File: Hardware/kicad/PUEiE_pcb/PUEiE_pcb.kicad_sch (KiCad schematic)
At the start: 11 parts, among them J1 Screw_Terminal_01x02, SW1 SW_DPDT_x2, U1 LM2675M-3.3, U2 MAX-M10S

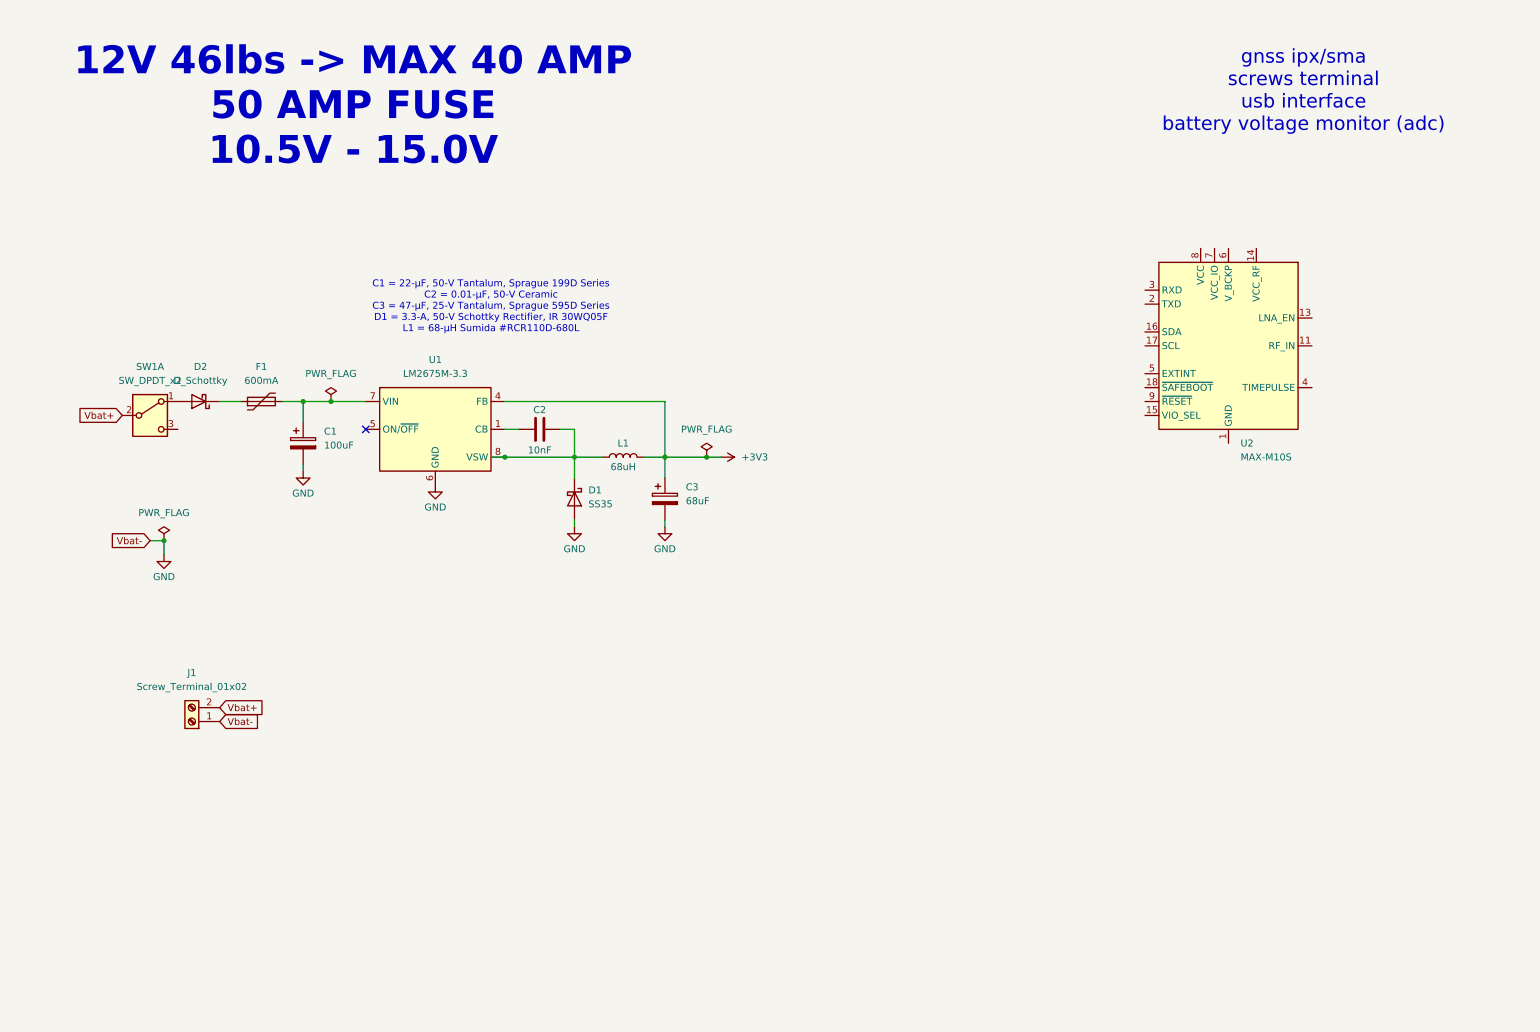
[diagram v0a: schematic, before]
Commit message: tps563240, GNSS
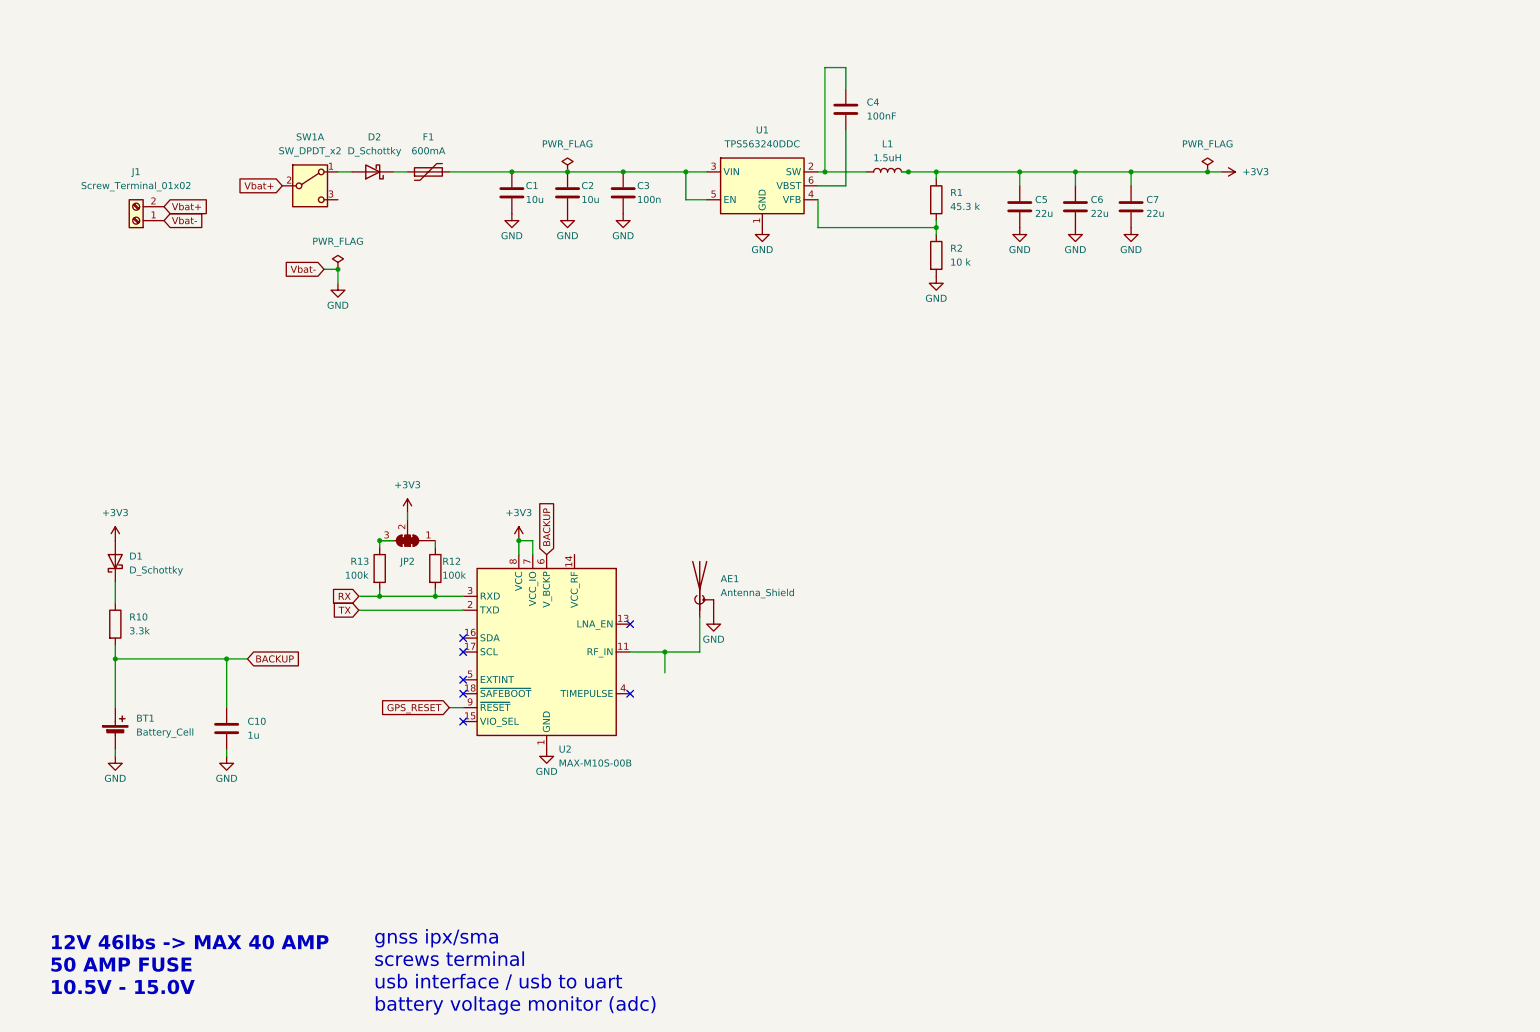
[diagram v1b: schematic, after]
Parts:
- removed C1: 100uF, symbol Device:C_Polarized
- removed C3: 68uF, symbol Device:C_Polarized
- removed D1: SS35, Diode_SMD:D_SMA, symbol Diode:SS35
- removed U1: LM2675M-3.3, Package_SO:SOIC-8_3.9x4.9mm_P1.27mm, symbol Regulator_Switching:LM2675M-3.3
- added AE1: Antenna_Shield, symbol Device:Antenna_Shield
- added BT1: Battery_Cell, symbol Device:Battery_Cell
- added C1: 10u, Capacitor_SMD:C_0805_2012Metric, symbol Device:C
- added C10: 1u, Capacitor_SMD:C_0805_2012Metric, symbol Device:C
- added C3: 100n, Capacitor_SMD:C_0805_2012Metric, symbol Device:C
- added C4: 100nF, Capacitor_SMD:C_0603_1608Metric, symbol Device:C
- added C5, C6, C7: 22u, Capacitor_SMD:C_0603_1608Metric, symbol Device:C
- added D1: D_Schottky, Diode_SMD:D_SOD-882, symbol Device:D_Schottky
- added JP2: SolderJumper_3_Bridged123, symbol Jumper:SolderJumper_3_Bridged123
- added R1: 45.3 k, Resistor_SMD:R_0402_1005Metric, symbol Device:R
- added R10: 3.3k, Resistor_SMD:R_0805_2012Metric, symbol Device:R
- added R12, R13: 100k, Resistor_SMD:R_0805_2012Metric, symbol Device:R
- added R2: 10 k, Resistor_SMD:R_0201_0603Metric, symbol Device:R
- added U1: TPS563240DDC, Package_TO_SOT_SMD:SOT-23-6, symbol Regulator_Switching:TPS563240DDC
- C2: value 10nF -> 10u; footprint (none) -> Capacitor_SMD:C_0805_2012Metric
- L1: value 68uH -> 1.5uH; Link 1 (none) -> https://jlcpcb.com/partdetail/Sumida-104CDMCCDS1R5MC/C516064
- U2: value MAX-M10S -> MAX-M10S-00B; Link 1 (none) -> https://jlcpcb.com/partdetail/UBLOX-MAX_M10S00B/C4153167
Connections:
- net +3V3: now also U2.7 (VCC_IO), U2.8 (VCC), C5.1, C6.1, C7.1, D1.2 (A), JP2.2 (C), R1.1
- net GND: now also C2.2, U2.1 (GND), U2.10 (GND), U2.12 (GND), AE1.2 (Shield), BT1.2 (-), C1.2, C10.2, C3.2, C5.2, C6.2, C7.2, R2.2, U1.1 (GND)
- net at L1.1: now also C4.1, U1.2 (SW); no longer C2.2
- net at U2.11 (RF_IN): now also AE1.1 (A)
- net TX: now reaches U2.2 (TXD)
- net RX: now reaches U2.3 (RXD)
- net RX: now also R12.2, R13.2
- net BACKUP: now reaches U2.6 (V_BCKP)
- net BACKUP: now also BT1.1 (+), C10.1, R10.2
- net GPS_RESET: now reaches U2.9 (~{RESET})
- net at C2.1: now also F1.2, C1.1, C3.1, U1.3 (VIN), U1.5 (EN)
- new net: R1.2, R2.1, U1.4 (VFB)
- new net: C4.2, U1.6 (VBST)
- new net: D1.1 (K), R10.1
- new net: JP2.1 (A), R12.1
- new net: JP2.3 (B), R13.1
- no-connect marks 1 -> 7
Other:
- note added: "gnss ipx/sma screws terminal usb interface / usb to uart battery voltage monitor (adc)"
- note removed: "C1 = 22-μF, 50-V Tantalum, Sprague 199D Series C2 = 0.01-μF, 50-V Ceramic C3 = 47-μF, 25-V Tantalum, Sprague 595D Series D1 = 3.3-A, 50-V Schottky Rectifier, IR 30WQ05F L1 = 68-μH Sumida #RCR110D-680L"
- note removed: "gnss ipx/sma screws terminal usb interface battery voltage monitor (adc)"
- moved on the sheet: D2, F1, J1, SW1A, U2

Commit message: usbc
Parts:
- removed JP2: SolderJumper_3_Bridged123, symbol Jumper:SolderJumper_3_Bridged123
- added C8: 22uF, symbol Device:C
- added J2: USB_C_Receptacle_USB2.0_14P, symbol Connector:USB_C_Receptacle_USB2.0_14P
- added JP1: SolderJumper_3_Bridged123, symbol Jumper:SolderJumper_3_Bridged123
- added R3, R4: 5.1k, symbol Device:R
- added U3: USBLC6-2P6, Package_TO_SOT_SMD:SOT-666, symbol Power_Protection:USBLC6-2P6
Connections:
- net +3V3: now also JP1.2 (C)
- net GND: now also C8.1, J2.A1 (GND), J2.A12 (GND), J2.B1 (GND), J2.B12 (GND), J2.S1 (SHIELD), R3.2, R4.2, U3.2 (GND)
- net RX: no longer R12.2
- net TX: now also R12.2
- net at R12.1: now also JP1.1 (A)
- net at R13.1: now also JP1.3 (B)
- new net: C8.2, J2.A4 (VBUS), J2.A9 (VBUS), J2.B4 (VBUS), J2.B9 (VBUS)
- new net: J2.A5 (CC1), R4.1
- new net: J2.B5 (CC2), R3.1
- new net USB_D+: J2.A6 (D+), J2.B6 (D+), U3.1 (I/O1), U3.6 (I/O1)
- new net USB_D-: J2.A7 (D-), J2.B7 (D-), U3.3 (I/O2), U3.4 (I/O2)
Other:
- note added: "USB-C connector and ESD Protection"

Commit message: cleanup
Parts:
- removed AE1: Antenna_Shield, symbol Device:Antenna_Shield
- removed BT1: Battery_Cell, symbol Device:Battery_Cell
- removed C1, C2: 10u, Capacitor_SMD:C_0805_2012Metric, symbol Device:C
- removed C10: 1u, Capacitor_SMD:C_0805_2012Metric, symbol Device:C
- removed C3: 100n, Capacitor_SMD:C_0805_2012Metric, symbol Device:C
- removed C4: 100nF, Capacitor_SMD:C_0603_1608Metric, symbol Device:C
- removed C5, C6, C7: 22u, Capacitor_SMD:C_0603_1608Metric, symbol Device:C
- removed C8: 22uF, symbol Device:C
- removed D1: D_Schottky, Diode_SMD:D_SOD-882, symbol Device:D_Schottky
- removed D2: D_Schottky, symbol Device:D_Schottky
- removed F1: 600mA, symbol Device:Polyfuse
- removed J2: USB_C_Receptacle_USB2.0_14P, symbol Connector:USB_C_Receptacle_USB2.0_14P
- removed JP1: SolderJumper_3_Bridged123, symbol Jumper:SolderJumper_3_Bridged123
- removed L1: 1.5uH, symbol Device:L
- removed R1: 45.3 k, Resistor_SMD:R_0402_1005Metric, symbol Device:R
- removed R10: 3.3k, Resistor_SMD:R_0805_2012Metric, symbol Device:R
- removed R12, R13: 100k, Resistor_SMD:R_0805_2012Metric, symbol Device:R
- removed R2: 10 k, Resistor_SMD:R_0201_0603Metric, symbol Device:R
- removed SW1: SW_DPDT_x2, Button_Switch_THT:SW_E-Switch_EG1224_SPDT_Angled, symbol Switch:SW_DPDT_x2
- removed U1: TPS563240DDC, Package_TO_SOT_SMD:SOT-23-6, symbol Regulator_Switching:TPS563240DDC
- removed U2: MAX-M10S-00B, RF_GPS:ublox_MAX, symbol RF_GPS:MAX-M10S
- removed U3: USBLC6-2P6, Package_TO_SOT_SMD:SOT-666, symbol Power_Protection:USBLC6-2P6
- added J3: USB_C_Receptacle_USB2.0_16P, Connector_USB:USB_C_Receptacle_GCT_USB4105-xx-A_16P_TopMnt_Horizontal, symbol Connector:USB_C_Receptacle_USB2.0_16P
- added U3: USBLC6-2SC6, Package_TO_SOT_SMD:SOT-23-6, symbol Power_Protection:USBLC6-2SC6
- added U4: CH340E, Package_SO:MSOP-10_3x3mm_P0.5mm, symbol Interface_USB:CH340E
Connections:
- net GND: now also J3.A1 (GND), J3.A12 (GND), J3.B1 (GND), J3.B12 (GND), J3.S1 (SHIELD), U3.2 (GND); no longer J1.1 (Pin_1)
- net USB_D+: now also U3.6 (I/O1)
- net USB_D-: now also U3.4 (I/O2)
- net USBCC1: now reaches R4.1
- net USBCC1: now also J3.A5 (CC1)
- net USBCC2: now reaches R3.1
- net USBCC2: now also J3.B5 (CC2)
- net Vbat+ renamed +3.3V Regulator/Vbat+
- new net +3.3V Regulator/Vbat-: J1.1 (Pin_1)
- new net USBD+: J3.A6 (D+), J3.B6 (D+), U3.3 (I/O2)
- new net USBD-: J3.A7 (D-), J3.B7 (D-), U3.1 (I/O1)
- new net VUSB: J3.A4 (VBUS), J3.A9 (VBUS), J3.B4 (VBUS), J3.B9 (VBUS), U3.5 (VBUS)
- no-connect marks 7 -> 2
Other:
- added sheet +3.3V Regulator (3_3V_Regulator.kicad_sch)
- added sheet Interfaces (Interfaces.kicad_sch)
- moved on the sheet: J1, R3, R4

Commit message: Vbat
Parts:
- removed U4: CH340E, Package_SO:MSOP-10_3x3mm_P0.5mm, symbol Interface_USB:CH340E
- added U4: DRV8461SPWP, Package_SO:Texas_PWP0020A, symbol Driver_Motor:DRV8461SPWP
- added U6: LIS3MDL, Package_LGA:LGA-12_2x2mm_P0.5mm, symbol Sensor_Magnetic:LIS3MDL
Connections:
- new net: U4.10 (BOUT1), U4.11 (BOUT1)
- new net: U4.12 (GND), U4.14 (GND), U4.29 (GND), U4.3 (GND)
- new net: U4.13 (VM), U4.2 (VM)
- new net: U4.4 (AOUT1), U4.5 (AOUT1)
- new net: U4.6 (AOUT2), U4.7 (AOUT2)
- new net: U4.8 (BOUT2), U4.9 (BOUT2)
- new net: U6.12 (GND), U6.2 (GND), U6.3 (GND)
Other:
- note added: "gnss ipx/sma screws terminal usb interface / usb to uart battery voltage monitor (adc) stm32 magnetometr i sterownik do silnika krokowego"
- note removed: "gnss ipx/sma screws terminal usb interface / usb to uart battery voltage monitor (adc)"
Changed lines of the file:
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@@
 		)
 	)
-	(text "gnss ipx/sma\nscrews terminal\nusb interface / usb to uart\nbattery voltage monitor (adc)"
+	(text "gnss ipx/sma\nscrews terminal\nusb interface / usb to uart\nbattery voltage monitor (adc)\n\nstm32\nmagnetometr\ni sterownik do silnika krokowego"
 		(exclude_from_sim no)
-		(at 88.646 23.114 0)
+		(at 85.344 29.718 0)
 		(effects
 			(font
@@
 	)
 	(symbol
+		(lib_id "Driver_Motor:DRV8461SPWP")
+		(at 189.23 86.36 0)
+		(unit 1)
+		(exclude_from_sim no)
+		(in_bom yes)
+		(on_board yes)
+		(dnp no)
+		(fields_autoplaced yes)
+		(property "Reference" "U4"
+			(at 191.3733 109.22 0)
+			(effects
+				(font
+					(size 1.27 1.27)
+				)
+				(justify left)
+			)
+		)
+		(property "Value" "DRV8461SPWP"
+			(at 191.3733 111.76 0)
+			(effects
+				(font
+					(size 1.27 1.27)
+				)
+				(justify left)
+			)
+		)
+		(property "Footprint" "Package_SO:Texas_PWP0020A"
+			(at 209.55 113.03 0)
+			(effects
+				(font
+					(size 1.27 1.27)
+				)
+				(justify left)
+				(hide yes)
+			)
+		)
+		(property "Datasheet" "https://www.ti.com/lit/ds/symlink/drv8461.pdf"
+			(at 209.55 115.57 0)
+			(effects
+				(font
+					(size 1.27 1.27)
+				)
+				(justify left)
+				(hide yes)
+			)
+		)
+		(property "Description" "65V, 3A SPI Stepper motor controller with integrated MOSFETs, automatic torque, automatic microstep, HTSSOP-28"
+			(at 189.23 86.36 0)
+			(effects
+				(font
+					(size 1.27 1.27)
+				)
+				(hide yes)
+			)
+		)
+		(pin "18"
+		)
+		(pin "22"
+		)
+		(pin "15"
+		)
+		(pin "4"
+		)
+		(pin "9"
+		)
+		(pin "5"
+		)
+		(pin "21"
+		)
+		(pin "23"
+		)
+		(pin "26"
+		)
+		(pin "8"
+		)
+		(pin "27"
+		)
+		(pin "13"
+		)
+		(pin "12"
+		)
+		(pin "19"
+		)
+		(pin "16"
+		)
+		(pin "3"
+		)
+		(pin "17"
+		)
+		(pin "28"
+		)
+		(pin "2"
+		)
+		(pin "20"
+		)
+		(pin "7"
+		)
+		(pin "24"
+		)
+		(pin "25"
+		)
+		(pin "6"
+		)
+		(pin "10"
+		)
+		(pin "1"
+		)
+		(pin "14"
+		)
+		(pin "11"
+		)
+		(pin "29"
+		)
+		(instances
+			(project ""
+				(path "/064b0dc2-c3a5-4c74-8cbf-4fc3d8c84854"
+					(reference "U4")
+					(unit 1)
+				)
+			)
+		)
+	)
+	(symbol
 		(lib_id "Device:R")
 		(at 57.15 154.94 90)
@@
 	)
 	(symbol
-		(lib_id "Interface_USB:CH340E")
-		(at 252.73 143.51 0)
+		(lib_id "Sensor_Magnetic:LIS3MDL")
+		(at 199.39 31.75 0)
 		(unit 1)
 		(exclude_from_sim no)
@@
 		(on_board yes)
 		(dnp no)
-		(property "Reference" "U4"
-			(at 257.556 129.54 0)
+		(fields_autoplaced yes)
+		(property "Reference" "U6"
+			(at 201.5333 44.45 0)
 			(effects
 				(font
@@
 			)
 		)
-		(property "Value" "CH340E"
-			(at 252.984 157.48 0)
+		(property "Value" "LIS3MDL"
+			(at 201.5333 46.99 0)
 			(effects
 				(font
@@
 			)
 		)
-		(property "Footprint" "Package_SO:MSOP-10_3x3mm_P0.5mm"
-			(at 254 157.48 0)
-			(effects
-				(font
-					(size 1.27 1.27)
-				)
-				(justify left)
-				(hide yes)
-			)
-		)
-		(property "Datasheet" "https://www.mpja.com/download/35227cpdata.pdf"
-			(at 243.84 123.19 0)
-			(effects
-				(font
-					(size 1.27 1.27)
-				)
-				(hide yes)
-			)
-		)
-		(property "Description" "USB serial converter, UART, MSOP-10"
-			(at 252.73 143.51 0)
-			(effects
-				(font
-					(size 1.27 1.27)
-				)
-				(hide yes)
-			)
-		)
-		(property "Link 1" "https://jlcpcb.com/parts/componentSearch?searchTxt=ch340e"
-			(at 252.73 143.51 0)
-			(effects
-				(font
-					(size 1.27 1.27)
-				)
-				(hide yes)
-			)
+		(property "Footprint" "Package_LGA:LGA-12_2x2mm_P0.5mm"
+			(at 229.87 39.37 0)
+			(effects
+				(font
+					(size 1.27 1.27)
+				)
+				(hide yes)
+			)
+		)
+		(property "Datasheet" "https://www.st.com/resource/en/datasheet/lis3mdl.pdf"
+			(at 237.49 41.91 0)
+			(effects
+				(font
+					(size 1.27 1.27)
+				)
+				(hide yes)
+			)
+		)
+		(property "Description" "Ultra-low-power, 3-axis digital output magnetometer, LGA-12"
+			(at 199.39 31.75 0)
+			(effects
+				(font
+					(size 1.27 1.27)
+				)
+				(hide yes)
+			)
+		)
+		(property "Link 1" "https://jlcpcb.com/partdetail/STMicroelectronics-LIS3MDLTR/C478483"
+			(at 199.39 31.75 0)
+			(effects
+				(font
+					(size 1.27 1.27)
+				)
+				(hide yes)
+			)
+		)
+		(pin "5"
+		)
+		(pin "11"
+		)
+		(pin "9"
+		)
+		(pin "7"
+		)
+		(pin "10"
 		)
 		(pin "2"
 		)
-		(pin "5"
-		)
-		(pin "10"
+		(pin "4"
+		)
+		(pin "12"
+		)
+		(pin "8"
+		)
+		(pin "6"
 		)
 		(pin "1"
 		)
-		(pin "7"
-		)
 		(pin "3"
-		)
-		(pin "8"
-		)
-		(pin "9"
-		)
-		(pin "6"
-		)
-		(pin "4"
 		)
 		(instances
 			(project ""
 				(path "/064b0dc2-c3a5-4c74-8cbf-4fc3d8c84854"
-					(reference "U4")
+					(reference "U6")
 					(unit 1)
 				)
